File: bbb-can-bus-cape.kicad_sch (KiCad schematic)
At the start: 2 parts, among them P8 BeagleBone_Black_Header, P9 BeagleBone_Black_Header

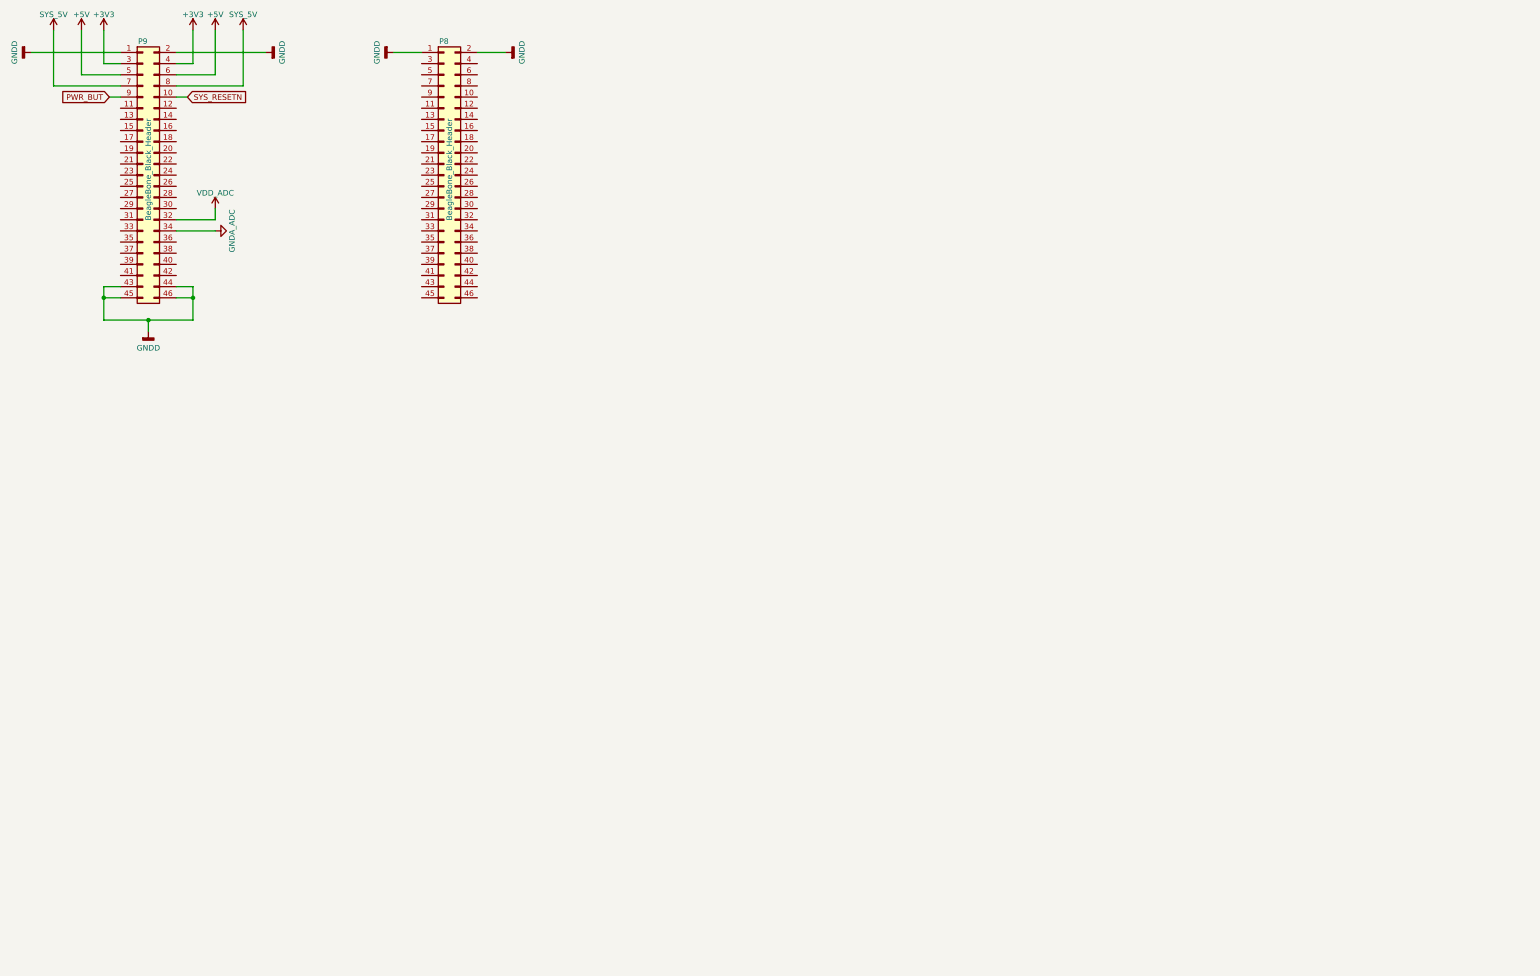
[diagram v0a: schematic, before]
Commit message: Added elements and hierarchical sheets
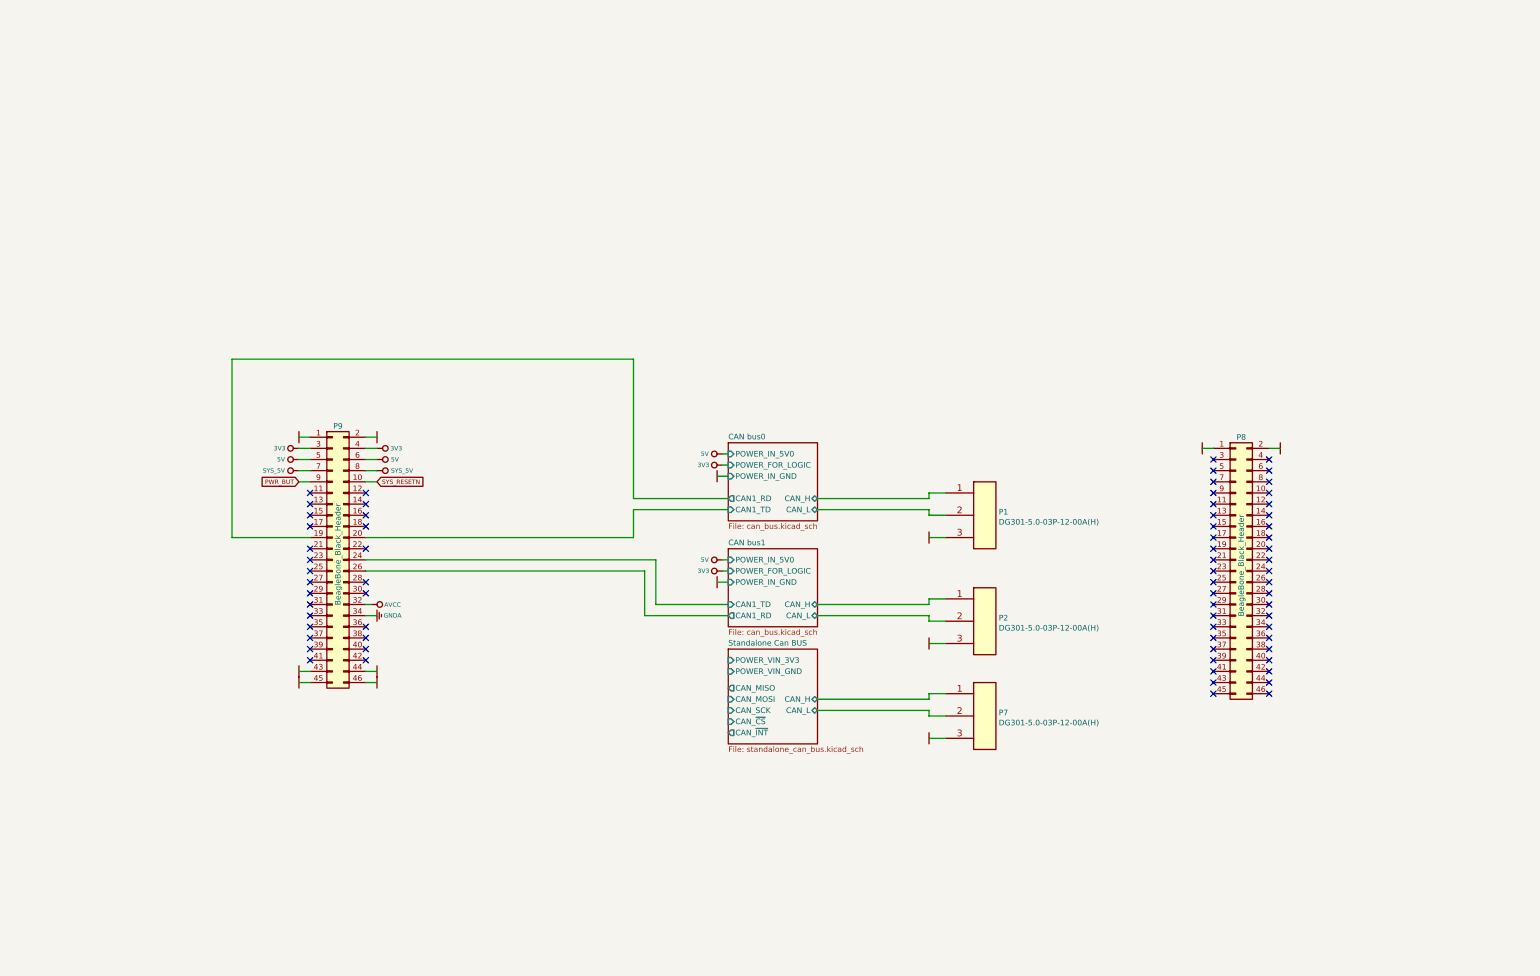
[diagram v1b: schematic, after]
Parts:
- added P1, P2, P7: DG301-5.0-03P-12-00A(H), Discrete_Connectors:DG301-5.0-03P-12-00A(H), symbol Discrete_Connectors:DG301-5.0-03P-12-00A(H)
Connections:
- net CAN bus0/CAN1_RD: now reaches P9.19 (Pin_19)
- net CAN bus0/CAN1_TD: now reaches P9.20 (Pin_20)
- net CAN bus1/CAN1_TD: now reaches P9.24 (Pin_24)
- net CAN bus1/CAN1_RD: now reaches P9.26 (Pin_26)
- net +3V3 renamed 3V3
- net +5V renamed 5V
- net GNDA_ADC renamed GNDA
- net GNDD renamed GND
- net GND: now also P1.3, P2.3, P7.3
- net VDD_ADC renamed VCC-RTC
- new net CAN bus0/CAN_H: P1.1
- new net CAN bus0/CAN_L: P1.2
- new net CAN bus1/CAN_H: P2.1
- new net CAN bus1/CAN_L: P2.2
- new net Standalone Can BUS/CAN_H: P7.1
- new net Standalone Can BUS/CAN_L: P7.2
- no-connect marks 0 -> 70
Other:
- added sheet CAN bus0 (can_bus.kicad_sch)
- added sheet CAN bus1 (can_bus.kicad_sch)
- added sheet Standalone Can BUS (standalone_can_bus.kicad_sch)
- company: (none) -> Embedded System Labs
- title: (none) -> Beaglebone Black CAN bus cape
- moved on the sheet: P8, P9

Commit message: Schematic checked
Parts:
- added C11, C12: 100n_50V, Capacitors_Smd_0603:100nF_0603, symbol Capacitors_Smd0603:100n
- added D10: LED_KP-2012HD, Diodes:LED_KP-2012HD_SM0805, symbol Diodes:LED_KP-2012HD
- added D11: LED_KP-2012SGD, Diodes:LED_KP-2012SGD_SM0805, symbol Diodes:LED_KP-2012SGD
- added D12: LED_KP-2012YD, Diodes:LED_KP-2012YD_SM0805, symbol Diodes:LED_KP-2012YD
- added NTC1: NTCS0603E3103FMT, NTC_Thermistors:NTCS0603E3103FMT, symbol NTC_Thermistors:NTCS0603E3103FMT
- added R11, R12, R16, R17, R18, R19: 4k7, Resistor_Smd_0603:4k7_0603, symbol Resistors_Smd0603:4k7
- added R13, R14, R15: 100R, Resistor_Smd_0603:100R_0603, symbol Resistors_Smd0603:100R
- added Sw1, Sw2: DTSM-31N, Microswitches:DTSM-31N_SMD, symbol Microswitches:DTSM-31N
- added U5: TCN75A, Temperature_Sensors:TCN75A_SOIC8, symbol Temperature_Sensors:TCN75A
- added U6: DS18B20U, Temperature_Sensors:DS18B20U_MSOP-8_3x3mm_P0.65mm, symbol Temperature_Sensors:DS18B20U
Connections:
- net 3V3: now also C11.1, C12.1, NTC1.2, R12.1, R16.1, R17.1, R18.1, R19.1, U5.7 (A0), U5.8 (VDD), U6.8 (VDD)
- net GND: now also C11.2, C12.2, D10.1 (A), D11.1 (A), D12.1 (A), R11.2, Sw1.2, Sw2.2, U5.4 (VSS), U5.5 (A2), U5.6 (A1), U6.4 (VSS)
- net PWR_BUT: now also R12.2, Sw1.1
- net SYS_RESETN: now also R16.2, Sw2.1
- net at P9.15 (Pin_15): now also R18.2, U6.1 (DQ)
- net I2C1_SCL: now reaches P9.17 (Pin_17)
- net I2C1_SCL: now also R17.2, U5.2 (SCL)
- net I2C1_SDA: now reaches P9.18 (Pin_18)
- net I2C1_SDA: now also R19.2, U5.1 (SDA)
- net SPI1_CS0: now reaches P9.28 (Pin_28)
- net SPI1_MISO: now reaches P9.29 (Pin_29)
- net SPI1_MOSI: now reaches P9.30 (Pin_30)
- net SPI1_SCK: now reaches P9.31 (Pin_31)
- net at P9.36 (Pin_36): now also R13.1
- net at P9.38 (Pin_38): now also R14.1
- net AN0: now reaches P9.39 (Pin_39)
- net AN0: now also NTC1.1, R11.1
- net at P9.40 (Pin_40): now also R15.1
- net GPIO0_20: now reaches P9.41 (Pin_41)
- net CAN bus0/CAN1_RD renamed DCAN0_RX
- net CAN bus0/CAN1_TD renamed DCAN0_TX
- net CAN bus1/CAN1_RD renamed DCAN1_TX
- net CAN bus1/CAN1_TD renamed DCAN1_RX
- new net: D11.2 (K), R14.2
- new net: D10.2 (K), R13.2
- new net: D12.2 (K), R15.2
- no-connect marks 70 -> 59
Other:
- moved on the sheet: P1, P2, P7, P8, P9

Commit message: Finalized project
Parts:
- added P12: RS485, Discrete_Connectors:DG301-5.0-03P-12-00A(H), symbol Discrete_Connectors:DG301-5.0-03P-12-00A(H)
- added P15: MCP2512-CAN, Discrete_Connectors:DG301-5.0-03P-12-00A(H), symbol Discrete_Connectors:DG301-5.0-03P-12-00A(H)
- added R28, R29: 4k7, Resistor_Smd_0603:4k7_0603, symbol Resistors_Smd0603:4k7
- added R30, R31: 100R, Resistor_Smd_0603:100R_0603, symbol Resistors_Smd0603:100R
- added Sw3, Sw4: DTSM-31N, Microswitches:DTSM-31N_SMD, symbol Microswitches:DTSM-31N
- P1: value DG301-5.0-03P-12-00A(H) -> BBB-DCAN0
- P2: value DG301-5.0-03P-12-00A(H) -> BBB-DCAN1
- P7: value DG301-5.0-03P-12-00A(H) -> MCP2515-CAN
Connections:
- net 3V3: now also R28.1, R29.1
- net GND: now also P12.3, P15.3, Sw3.2, Sw4.2
- net UART4_RX: now reaches P9.11 (Pin_11)
- net GPIO1_28: now reaches P9.12 (Pin_12)
- net UART4_TX: now reaches P9.13 (Pin_13)
- net GPIO1_17: now reaches P9.21 (Pin_21)
- net GPIO1_17: now also R30.2
- net GPIO3_21: now reaches P9.23 (Pin_23)
- net GPIO3_21: now also R31.2
- net Standalone Can BUS/CAN_~INT1~: now reaches P9.27 (Pin_27)
- net AIN5: now reaches P9.36 (Pin_36), R13.1
- net AIN3: now reaches P9.38 (Pin_38), R14.1
- net AIN1: now reaches P9.40 (Pin_40), R15.1
- net SPI1_CS1: now reaches P9.42 (Pin_42)
- net Standalone Can BUS/CAN_H renamed Standalone Can BUS/CAN_H0
- net Standalone Can BUS/CAN_L renamed Standalone Can BUS/CAN_L0
- new net: R29.2, R31.1, Sw4.1
- new net: R28.2, R30.1, Sw3.1
- new net RS485/RS485_A: P12.1
- new net RS485/RS485_B: P12.2
- new net Standalone Can BUS/CAN_H1: P15.1
- new net Standalone Can BUS/CAN_L1: P15.2
- no-connect marks 59 -> 52
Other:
- added sheet RS485 (rs485.kicad_sch)
- sheet Standalone Can BUS ports: added CAN_H0, CAN_H1, CAN_L0, CAN_L1, CAN_~CS0~, CAN_~CS1~, CAN_~INT0~, CAN_~INT1~, POWER_VIN_5V0; removed CAN_H, CAN_L, CAN_~CS~, CAN_~INT~
- moved on the sheet: C11, C12, D10, D11, D12, NTC1, P1, P2, P7, P8, P9, R11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

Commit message: Finalized project
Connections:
- net GPIO1_17: now also P9.23 (Pin_23), R13.1; no longer P9.21 (Pin_21), R30.2
- net GPIO3_21: now also P9.25 (Pin_25), R15.1; no longer P9.23 (Pin_23), R31.2
- net GPIO0_2: now reaches P9.22 (Pin_22)
- net GPIO0_2: now also R14.1
- net at P9.37 (Pin_37): now also R31.2
- net AIN1: no longer names the net of P9.40 (Pin_40)
- net AIN1: no longer R15.1
- net AIN3: no longer names the net of P9.38 (Pin_38)
- net AIN3: no longer R14.1
- net AIN5: no longer names the net of P9.36 (Pin_36)
- net AIN5: no longer R13.1
- new net GPIO0_3: P9.21 (Pin_21), R30.2
- no-connect marks 52 -> 51
